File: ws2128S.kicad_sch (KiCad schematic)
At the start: 12 parts

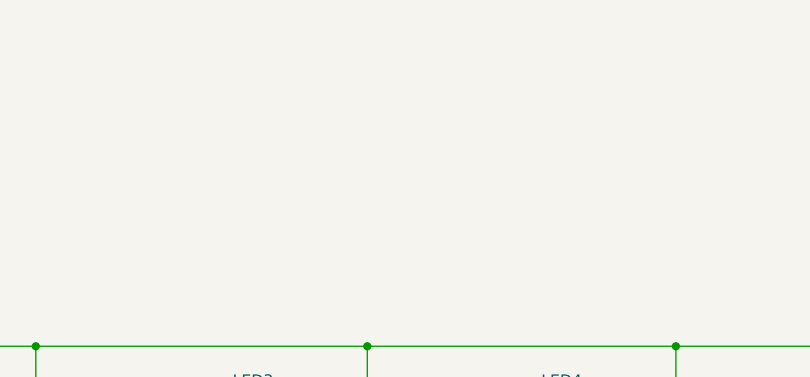
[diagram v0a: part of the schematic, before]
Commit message: updated titles and changes to wires
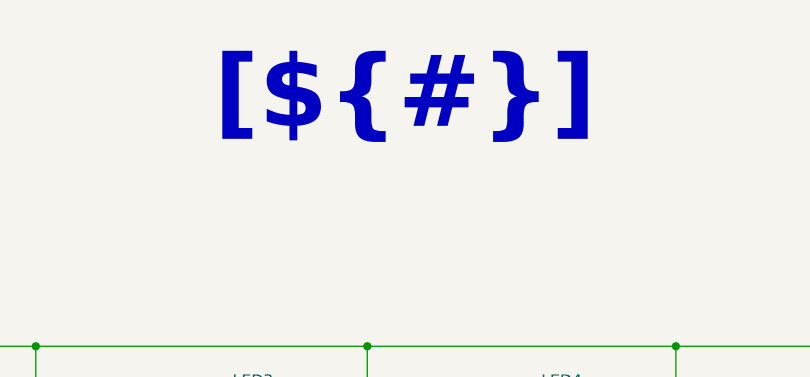
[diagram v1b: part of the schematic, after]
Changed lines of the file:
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@@
 	(generator_version "9.0")
 	(paper "A4")
+	(text_box "[${#}] ${TITLE}"
+		(exclude_from_sim no)
+		(at 92.456 14.986 0)
+		(size 130.81 12.7)
+		(margins 5.9999 5.9999 5.9999 5.9999)
+		(stroke
+			(width -0.0001)
+			(type default)
+		)
+		(fill
+			(type none)
+		)
+		(effects
+			(font
+				(face "Times New Roman")
+				(size 8 8)
+				(thickness 1.2)
+				(bold yes)
+				(color 162 22 34 1)
+			)
+		)
+	)
 	(junction
 		(at 128.27 73.66)

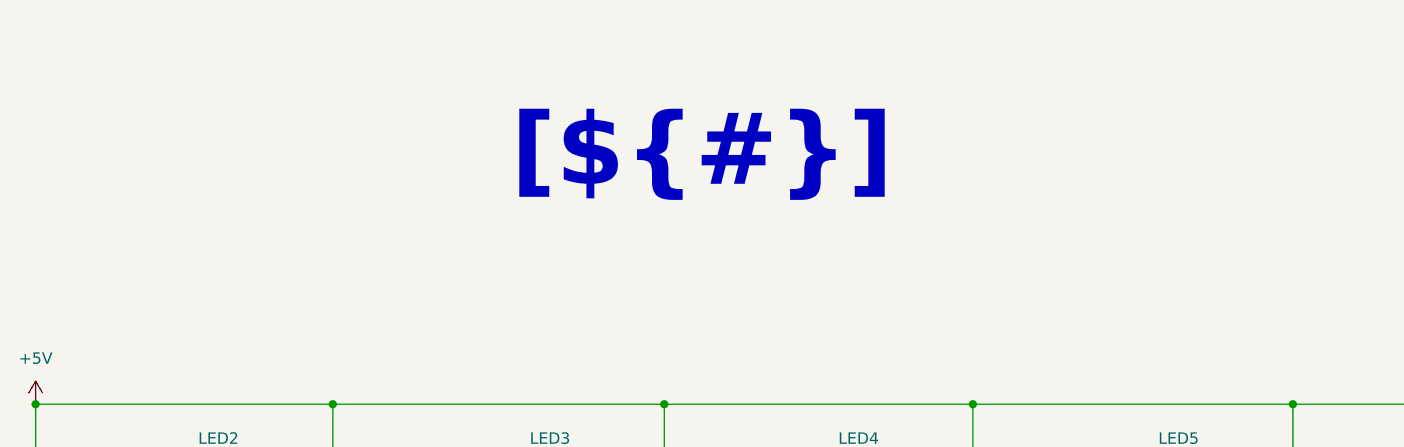
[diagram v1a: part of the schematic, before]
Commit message: updated titles and changes to wires
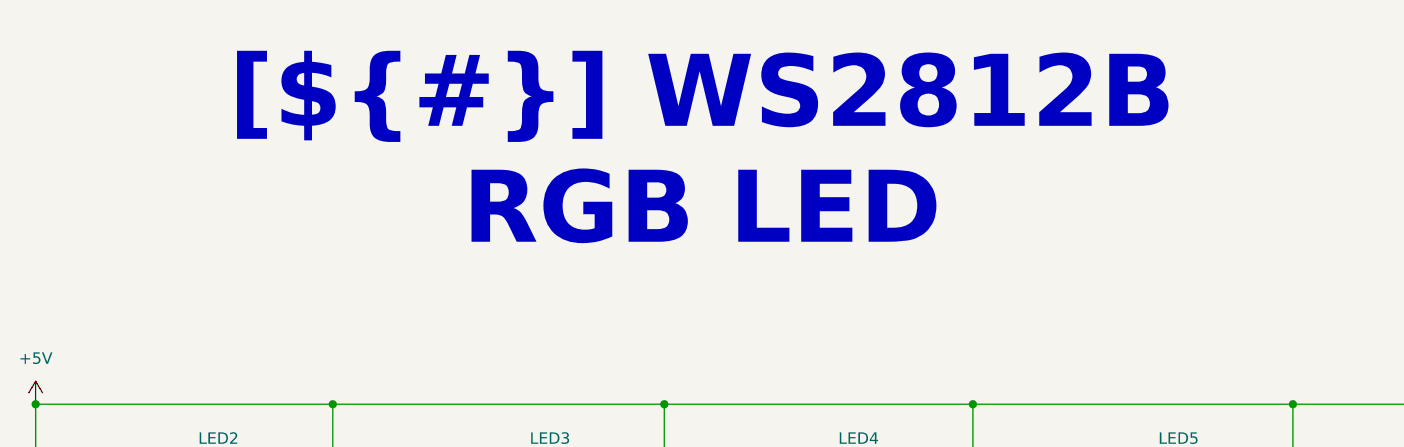
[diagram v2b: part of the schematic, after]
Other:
- title: (none) -> WS2812B RGB LED
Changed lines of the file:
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@@
 	(generator_version "9.0")
 	(paper "A4")
+	(title_block
+		(title "WS2812B RGB LED")
+	)
 	(text_box "[${#}] ${TITLE}"
 		(exclude_from_sim no)
